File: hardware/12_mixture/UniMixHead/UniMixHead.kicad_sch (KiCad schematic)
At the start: 28 parts, among them IC1 AP7375-50W5-7, J10 Conn_01x02_Male, J11 Conn_01x02_Male, J12 Conn_01x02_Male, J13 Conn_01x03_Pin, J14 Conn_01x03_Pin, J16 Conn_01x04_Male, J17 Conn_01x04_Male, J19 Conn_01x04_Male, J25 Conn_01x04_Male, J26 Conn_01x04_Male, J27 Conn_01x04_Male, J28 Conn_01x04_Male, J29 Conn_01x04_Male, J30 Conn_01x04_Male, U10 XGZP6847A, U9 XGZP6847A

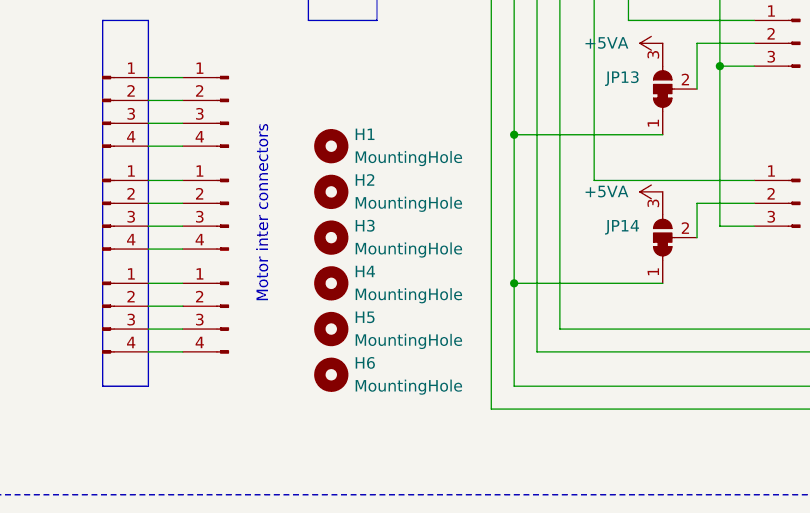
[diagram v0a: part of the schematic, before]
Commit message: Upadtes for Nucleo version
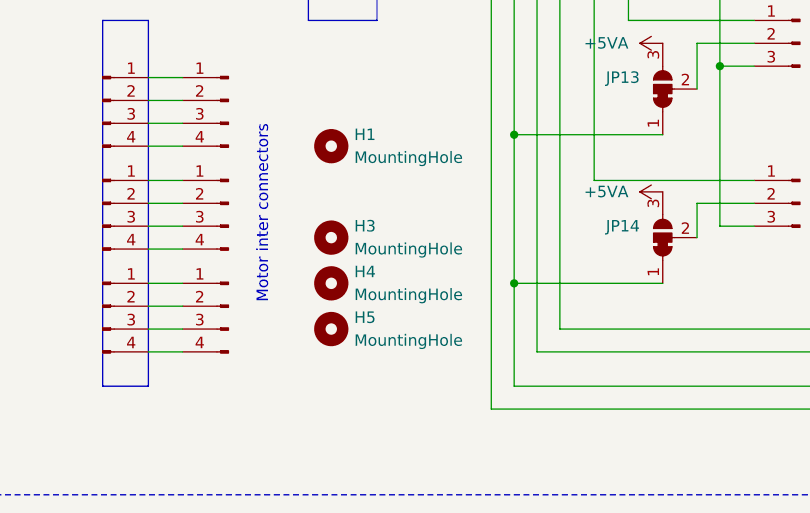
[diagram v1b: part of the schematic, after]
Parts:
- removed H2, H6: MountingHole, MountingHole:MountingHole_3.2mm_M3, symbol Mechanical:MountingHole
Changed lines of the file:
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@@
-	)
-	(symbol
-		(lib_id "Mechanical:MountingHole")
-		(at 92.71 125.73 0)
-		(unit 1)
-		(exclude_from_sim yes)
-		(in_bom no)
-		(on_board yes)
-		(dnp no)
-		(fields_autoplaced yes)
-		(property "Reference" "H6"
-			(at 95.25 124.4599 0)
-			(effects
-				(font
-					(size 1.27 1.27)
-				)
-				(justify left)
-			)
-		)
-		(property "Value" "MountingHole"
-			(at 95.25 126.9999 0)
-			(effects
-				(font
-					(size 1.27 1.27)
-				)
-				(justify left)
-			)
-		)
-		(property "Footprint" "MountingHole:MountingHole_3.2mm_M3"
-			(at 92.71 125.73 0)
-			(effects
-				(font
-					(size 1.27 1.27)
-				)
-				(hide yes)
-			)
-		)
-		(property "Datasheet" "~"
-			(at 92.71 125.73 0)
-			(effects
-				(font
-					(size 1.27 1.27)
-				)
-				(hide yes)
-			)
-		)
-		(property "Description" "Mounting Hole without connection"
-			(at 92.71 125.73 0)
-			(effects
-				(font
-					(size 1.27 1.27)
-				)
-				(hide yes)
-			)
-		)
-		(instances
-			(project "UniMixHead"
-				(path "/f56802d9-f699-4746-9270-4bac50efc0a1"
-					(reference "H6")
-					(unit 1)
-				)
-			)
-		)
 	)
 	(symbol
@@
 					(unit 1)
 				)
-			)
-		)
-	)
-	(symbol
-		(lib_id "Mechanical:MountingHole")
-		(at 92.71 105.41 0)
-		(unit 1)
-		(exclude_from_sim yes)
-		(in_bom no)
-		(on_board yes)
-		(dnp no)
-		(fields_autoplaced yes)
-		(property "Reference" "H2"
-			(at 95.25 104.1399 0)
-			(effects
-				(font
-					(size 1.27 1.27)
-				)
-				(justify left)
-			)
-		)
-		(property "Value" "MountingHole"
-			(at 95.25 106.6799 0)
-			(effects
-				(font
-					(size 1.27 1.27)
-				)
-				(justify left)
-			)
-		)
-		(property "Footprint" "MountingHole:MountingHole_3.2mm_M3"
-			(at 92.71 105.41 0)
-			(effects
-				(font
-					(size 1.27 1.27)
-				)
-				(hide yes)
-			)
-		)
-		(property "Datasheet" "~"
-			(at 92.71 105.41 0)
-			(effects
-				(font
-					(size 1.27 1.27)
-				)
-				(hide yes)
-			)
-		)
-		(property "Description" "Mounting Hole without connection"
-			(at 92.71 105.41 0)
-			(effects
-				(font
-					(size 1.27 1.27)
-				)
-				(hide yes)
-			)
-		)
-		(instances
-			(project "UniMixHead"
-				(path "/f56802d9-f699-4746-9270-4bac50efc0a1"
-					(reference "H2")
-					(unit 1)
-				)
